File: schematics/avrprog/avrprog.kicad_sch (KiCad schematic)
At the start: 37 parts, among them J1 USB_B, J2 AVR-ISP-10, J3 PROG_PWR, J4 EMCLK, J5 SELF_PROG, U1 FT232RL, U2 ATmega8A-P, Y1 16MHz

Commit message: schematic ...
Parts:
- D8: value PPWRLED -> PWRLED
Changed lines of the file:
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@@
   (junction (at 180.34 43.18) (diameter 0) (color 0 0 0 0)
+  )
+  (junction (at 35.56 67.31) (diameter 0) (color 0 0 0 0)
   )
   (junction (at 196.85 27.94) (diameter 0) (color 0 0 0 0)
@@
     (pin "1")
   )
-  (symbol (lib_id "power:VCC") (at 52.07 69.85 0) (unit 1)
-    (in_bom yes) (on_board yes) (fields_autoplaced)
-    (property "Reference" "#PWR02" (id 0) (at 52.07 73.66 0)
-      (effects (font (size 1.27 1.27)) hide)
-    )
-    (property "Value" "VCC" (id 1) (at 52.07 64.77 0))
+  (symbol (lib_id "power:VCC") (at 52.07 69.85 270) (unit 1)
+    (in_bom yes) (on_board yes) (fields_autoplaced)
+    (property "Reference" "#PWR02" (id 0) (at 48.26 69.85 0)
+      (effects (font (size 1.27 1.27)) hide)
+    )
+    (property "Value" "VCC" (id 1) (at 55.88 69.8499 90)
+      (effects (font (size 1.27 1.27)) (justify left))
+    )
     (property "Footprint" "" (id 2) (at 52.07 69.85 0)
       (effects (font (size 1.27 1.27)) hide)
@@
     )
     (property "Datasheet" "" (id 3) (at 81.28 124.46 0)
+      (effects (font (size 1.27 1.27)) hide)
+    )
+    (pin "1")
+  )
+  (symbol (lib_id "power:PWR_FLAG") (at 35.56 67.31 0) (unit 1)
+    (in_bom yes) (on_board yes) (fields_autoplaced)
+    (property "Reference" "#FLG0102" (id 0) (at 35.56 65.405 0)
+      (effects (font (size 1.27 1.27)) hide)
+    )
+    (property "Value" "PWR_FLAG" (id 1) (at 38.1 66.0399 0)
+      (effects (font (size 1.27 1.27)) (justify left))
+    )
+    (property "Footprint" "" (id 2) (at 35.56 67.31 0)
+      (effects (font (size 1.27 1.27)) hide)
+    )
+    (property "Datasheet" "~" (id 3) (at 35.56 67.31 0)
       (effects (font (size 1.27 1.27)) hide)
     )
@@
       (effects (font (size 1.27 1.27)) (justify right))
     )
-    (property "Value" "PPWRLED" (id 1) (at 52.07 118.4274 90)
+    (property "Value" "PWRLED" (id 1) (at 52.07 118.4274 90)
       (effects (font (size 1.27 1.27)) (justify right))
     )
@@
       (reference "#FLG0101") (unit 1) (value "PWR_FLAG") (footprint "")
     )
+    (path "/51a1c586-d1f4-4b83-b720-2322c5faf689"
+      (reference "#FLG0102") (unit 1) (value "PWR_FLAG") (footprint "")
+    )
     (path "/b570ab2f-b9f6-411e-9c83-e8f97ef2f65d"
       (reference "#PWR01") (unit 1) (value "GND") (footprint "")
@@
     )
     (path "/be34b9bd-279e-4787-9dc2-e7492296784e"
-      (reference "D8") (unit 1) (value "PPWRLED") (footprint "LED_THT:LED_D3.0mm")
+      (reference "D8") (unit 1) (value "PWRLED") (footprint "LED_THT:LED_D3.0mm")
     )
     (path "/727ac96a-3f0b-4596-8661-4535112a64e9"

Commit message: schematic ...
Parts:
- added C10: 100nF, Capacitor_THT:C_Disc_D3.8mm_W2.6mm_P2.50mm, symbol Device:C
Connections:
- net GND: now also C10.1
- net VCC: now also C10.2
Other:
- moved on the sheet: C1, C3, C4, D8, R11

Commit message: schematics completed
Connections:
- net CTS_AT# renamed RTS_FT232#
- net RTS_FT232#: no longer U2.5 (PD3)
- net CTS_FT232#: no longer names the net of U1.11 (CTS)
- net CTS_FT232#: no longer U2.4 (PD2)
- net RXD_AT renamed TXD_FT232
- no-connect marks 15 -> 18
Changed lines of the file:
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@@
   (junction (at 196.85 27.94) (diameter 0) (color 0 0 0 0)
   )
+  (no_connect (at 214.63 105.41))
   (no_connect (at 116.84 69.85))
   (no_connect (at 116.84 87.63))
@@
   (no_connect (at 214.63 85.09))
   (no_connect (at 76.2 74.93))
+  (no_connect (at 214.63 107.95))
   (no_connect (at 214.63 82.55))
   (no_connect (at 214.63 64.77))
   (no_connect (at 214.63 110.49))
+  (no_connect (at 116.84 64.77))
   (no_connect (at 116.84 90.17))
   (no_connect (at 76.2 85.09))
@@
   (no_connect (at 214.63 69.85))
   (no_connect (at 76.2 80.01))
-  (wire (pts (xy 254 99.06) (xy 266.7 99.06))
-    (stroke (width 0) (type default) (color 0 0 0 0))
-  )
   (wire (pts (xy 254 76.2) (xy 256.54 76.2))
     (stroke (width 0) (type default) (color 0 0 0 0))
@@
     (stroke (width 0) (type default) (color 0 0 0 0))
   )
-  (wire (pts (xy 254 96.52) (xy 266.7 96.52))
-    (stroke (width 0) (type default) (color 0 0 0 0))
-  )
   (wire (pts (xy 254 81.28) (xy 256.54 81.28))
     (stroke (width 0) (type default) (color 0 0 0 0))
@@
   )
   (wire (pts (xy 172.72 35.56) (xy 172.72 43.18))
-    (stroke (width 0) (type default) (color 0 0 0 0))
-  )
-  (wire (pts (xy 254 101.6) (xy 266.7 101.6))
-    (stroke (width 0) (type default) (color 0 0 0 0))
-  )
-  (wire (pts (xy 254 93.98) (xy 266.7 93.98))
     (stroke (width 0) (type default) (color 0 0 0 0))
   )
@@
   (label "MOSI_AT" (at 266.7 78.74 0)
     (effects (font (size 1.27 1.27)) (justify left bottom))
-  )
-  (label "RTS_FT232#" (at 254 101.6 180)
-    (effects (font (size 1.27 1.27)) (justify right bottom))
   )
   (label "TXLED#" (at 116.84 82.55 0)
@@
     (effects (font (size 1.27 1.27)) (justify left bottom))
   )
-  (label "TXD_FT232" (at 254 93.98 180)
-    (effects (font (size 1.27 1.27)) (justify right bottom))
+  (label "TXD_FT232" (at 214.63 100.33 0)
+    (effects (font (size 1.27 1.27)) (justify left bottom))
   )
   (label "USB_D-" (at 76.2 67.31 180)
@@
     (effects (font (size 1.27 1.27)) (justify left bottom))
   )
-  (label "RTS_AT#" (at 214.63 105.41 0)
-    (effects (font (size 1.27 1.27)) (justify left bottom))
-  )
   (label "RXD_FT232" (at 254 76.2 180)
     (effects (font (size 1.27 1.27)) (justify right bottom))
@@
   (label "RTS_FT232#" (at 254 78.74 180)
     (effects (font (size 1.27 1.27)) (justify right bottom))
-  )
-  (label "TXD_AT" (at 266.7 96.52 0)
-    (effects (font (size 1.27 1.27)) (justify left bottom))
   )
   (label "SCK_PRG" (at 265.43 46.99 0)
@@
   )
   (label "RXLED#" (at 116.84 85.09 0)
-    (effects (font (size 1.27 1.27)) (justify left bottom))
-  )
-  (label "RXD_AT" (at 214.63 100.33 0)
     (effects (font (size 1.27 1.27)) (justify left bottom))
   )
@@
     (effects (font (size 1.27 1.27)) (justify left bottom))
   )
-  (label "CTS_FT232#" (at 116.84 64.77 0)
-    (effects (font (size 1.27 1.27)) (justify left bottom))
-  )
-  (label "CTS_AT#" (at 266.7 101.6 0)
-    (effects (font (size 1.27 1.27)) (justify left bottom))
-  )
   (label "EMCLK_AT" (at 214.63 67.31 0)
     (effects (font (size 1.27 1.27)) (justify left bottom))
@@
     (effects (font (size 1.27 1.27)) (justify left bottom))
   )
-  (label "RXD_AT" (at 266.7 93.98 0)
-    (effects (font (size 1.27 1.27)) (justify left bottom))
-  )
   (label "GREEN_AT" (at 214.63 118.11 0)
     (effects (font (size 1.27 1.27)) (justify left bottom))
@@
   (label "TXD_FT232" (at 116.84 57.15 0)
     (effects (font (size 1.27 1.27)) (justify left bottom))
-  )
-  (label "CTS_FT232#" (at 254 99.06 180)
-    (effects (font (size 1.27 1.27)) (justify right bottom))
   )
   (label "USB_D-" (at 35.56 72.39 0)
@@
     (effects (font (size 1.27 1.27)) (justify left bottom))
   )
-  (label "RXD_FT232" (at 254 96.52 180)
-    (effects (font (size 1.27 1.27)) (justify right bottom))
+  (label "RXD_FT232" (at 214.63 102.87 0)
+    (effects (font (size 1.27 1.27)) (justify left bottom))
   )
   (label "MOSI_PRG" (at 265.43 44.45 0)
-    (effects (font (size 1.27 1.27)) (justify left bottom))
-  )
-  (label "CTS_AT#" (at 214.63 107.95 0)
-    (effects (font (size 1.27 1.27)) (justify left bottom))
-  )
-  (label "TXD_AT" (at 214.63 102.87 0)
     (effects (font (size 1.27 1.27)) (justify left bottom))
   )
@@
     (effects (font (size 1.27 1.27)) (justify left bottom))
   )
-  (label "RTS_AT#" (at 266.7 99.06 0)
-    (effects (font (size 1.27 1.27)) (justify left bottom))
-  )

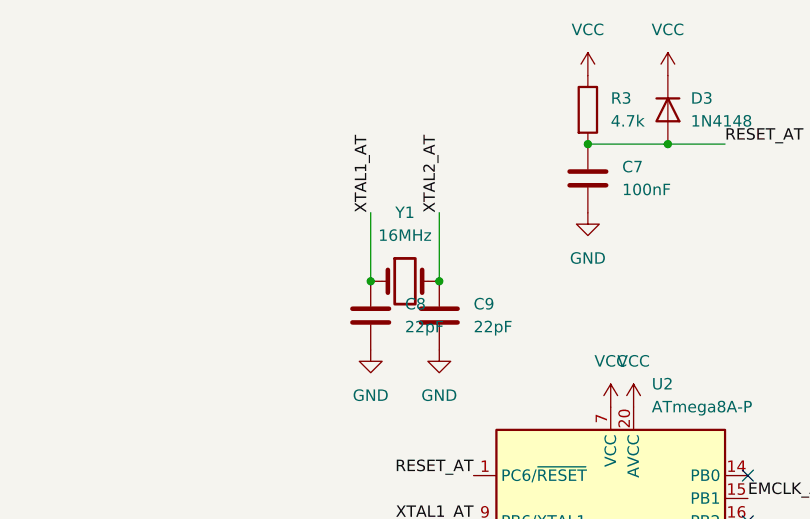
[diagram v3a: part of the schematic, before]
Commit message: crystal changed from 16MHz to 14.7456MHz due to USART communication
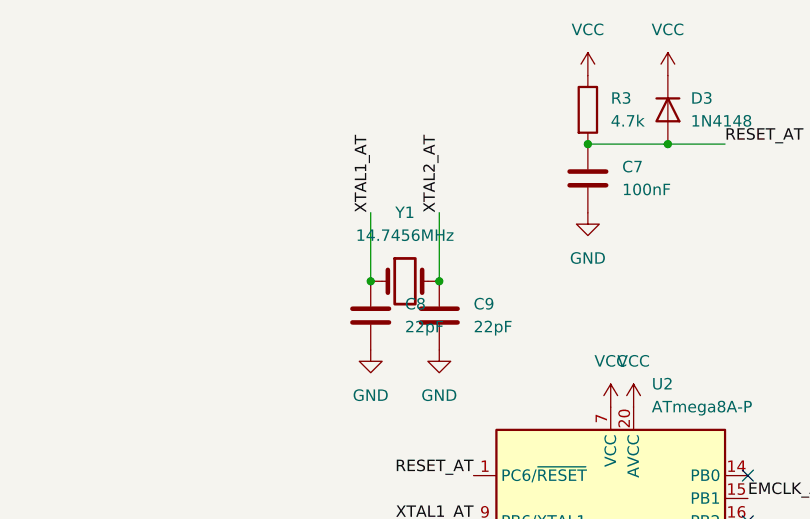
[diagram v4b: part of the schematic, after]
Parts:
- Y1: value 16MHz -> 14.7456MHz
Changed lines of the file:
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@@
     (in_bom yes) (on_board yes) (fields_autoplaced)
     (property "Reference" "Y1" (id 0) (at 176.53 35.56 0))
-    (property "Value" "16MHz" (id 1) (at 176.53 38.1 0))
+    (property "Value" "14.7456MHz" (id 1) (at 176.53 38.1 0))
     (property "Footprint" "Crystal:Crystal_HC49-U_Vertical" (id 2) (at 176.53 43.18 0)
       (effects (font (size 1.27 1.27)) hide)
     )
-    (property "Datasheet" "https://www.hestore.hu/prod_10021423.html" (id 3) (at 176.53 43.18 0)
+    (property "Datasheet" "https://www.hestore.hu/prod_10025226.html" (id 3) (at 176.53 43.18 0)
       (effects (font (size 1.27 1.27)) hide)
     )
@@
     )
     (path "/b62db5c2-6a16-4e7b-8e99-cc24d6f8d94d"
-      (reference "Y1") (unit 1) (value "16MHz") (footprint "Crystal:Crystal_HC49-U_Vertical")
-    )
-  )
+      (reference "Y1") (unit 1) (value "14.7456MHz") (footprint "Crystal:Crystal_HC49-U_Vertical")
+    )
+  )

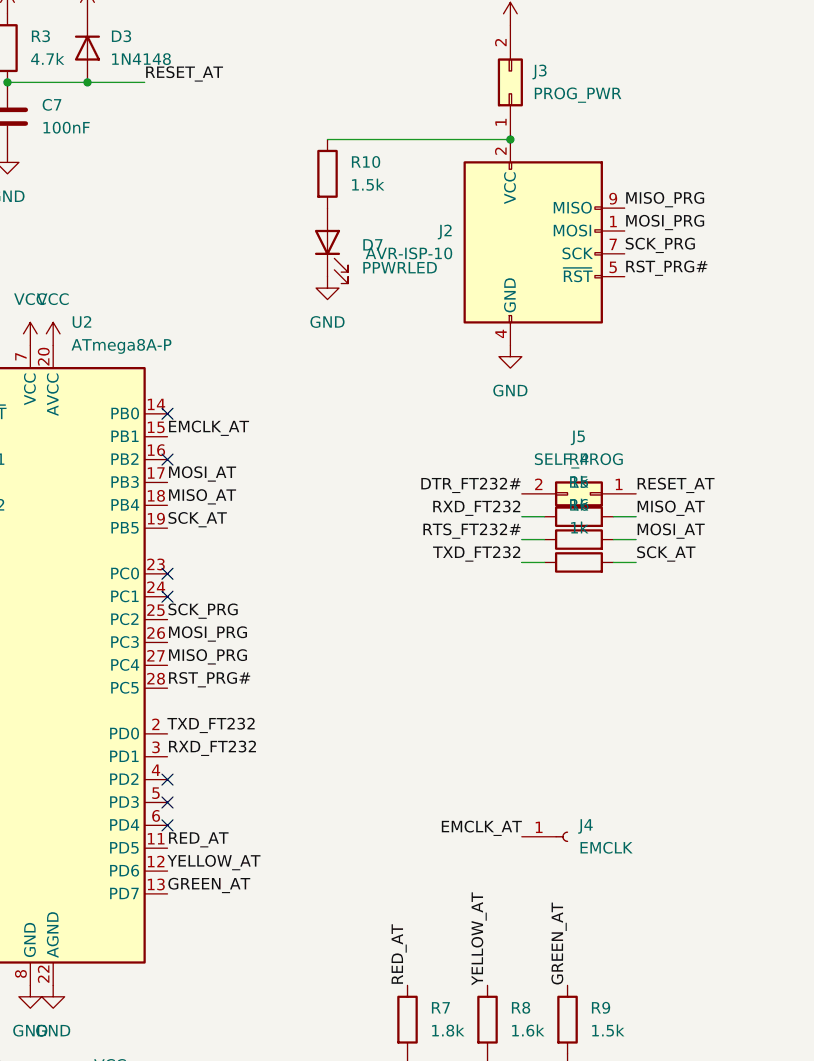
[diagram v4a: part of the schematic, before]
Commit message: PCB reorganized
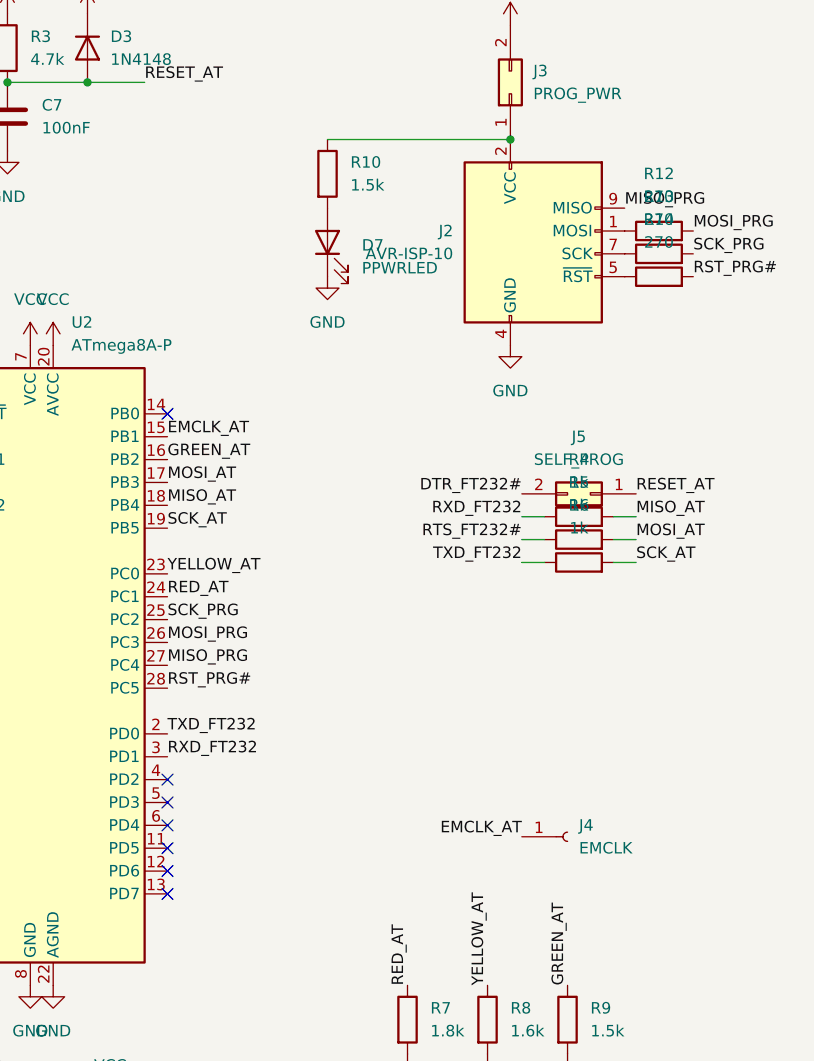
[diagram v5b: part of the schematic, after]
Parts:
- added R12, R13, R14: 270, Resistor_THT:R_Axial_DIN0207_L6.3mm_D2.5mm_P10.16mm_Horizontal, symbol Device:R
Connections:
- net GREEN_AT: now also U2.16 (PB2); no longer U2.13 (PD7)
- net MOSI_PRG: now also R12.2; no longer J2.1 (MOSI)
- net RED_AT: now also U2.24 (PC1); no longer U2.11 (PD5)
- net RST_PRG#: now also R14.2; no longer J2.5 (~{RST})
- net SCK_PRG: now also R13.2; no longer J2.7 (SCK)
- net YELLOW_AT: now also U2.23 (PC0); no longer U2.12 (PD6)
- new net: J2.7 (SCK), R13.1
- new net: J2.1 (MOSI), R12.1
- new net: J2.5 (~{RST}), R14.1
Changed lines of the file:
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@@
   (no_connect (at 184.15 80.01))
   (no_connect (at 116.84 74.93))
-  (no_connect (at 214.63 85.09))
+  (no_connect (at 214.63 115.57))
   (no_connect (at 76.2 74.93))
   (no_connect (at 214.63 107.95))
-  (no_connect (at 214.63 82.55))
+  (no_connect (at 214.63 113.03))
   (no_connect (at 214.63 64.77))
   (no_connect (at 214.63 110.49))
@@
   (no_connect (at 76.2 85.09))
   (no_connect (at 116.84 72.39))
-  (no_connect (at 214.63 69.85))
+  (no_connect (at 214.63 118.11))
   (no_connect (at 76.2 80.01))
   (wire (pts (xy 254 76.2) (xy 256.54 76.2))
@@
     (effects (font (size 1.27 1.27)) (justify left bottom))
   )
-  (label "YELLOW_AT" (at 214.63 115.57 0)
+  (label "YELLOW_AT" (at 214.63 82.55 0)
     (effects (font (size 1.27 1.27)) (justify left bottom))
   )
@@
     (effects (font (size 1.27 1.27)) (justify left bottom))
   )
-  (label "RED_AT" (at 214.63 113.03 0)
+  (label "RED_AT" (at 214.63 85.09 0)
     (effects (font (size 1.27 1.27)) (justify left bottom))
   )
@@
     (effects (font (size 1.27 1.27)) (justify left bottom))
   )
-  (label "RST_PRG#" (at 265.43 49.53 0)
+  (label "RST_PRG#" (at 273.05 49.53 0)
     (effects (font (size 1.27 1.27)) (justify left bottom))
   )
@@
     (effects (font (size 1.27 1.27)) (justify right bottom))
   )
-  (label "SCK_PRG" (at 265.43 46.99 0)
+  (label "SCK_PRG" (at 273.05 46.99 0)
     (effects (font (size 1.27 1.27)) (justify left bottom))
   )
@@
     (effects (font (size 1.27 1.27)) (justify left bottom))
   )
-  (label "GREEN_AT" (at 214.63 118.11 0)
+  (label "GREEN_AT" (at 214.63 69.85 0)
     (effects (font (size 1.27 1.27)) (justify left bottom))
   )
@@
     (effects (font (size 1.27 1.27)) (justify left bottom))
   )
-  (label "MOSI_PRG" (at 265.43 44.45 0)
+  (label "MOSI_PRG" (at 273.05 44.45 0)
     (effects (font (size 1.27 1.27)) (justify left bottom))
   )
@@
   (label "MISO_AT" (at 266.7 76.2 0)
     (effects (font (size 1.27 1.27)) (justify left bottom))
+  )
+  (symbol (lib_id "Device:R") (at 269.24 46.99 90) (unit 1)
+    (in_bom yes) (on_board yes) (fields_autoplaced)
+    (property "Reference" "R13" (id 0) (at 269.24 40.64 90))
+    (property "Value" "270" (id 1) (at 269.24 43.18 90))
+    (property "Footprint" "Resistor_THT:R_Axial_DIN0207_L6.3mm_D2.5mm_P10.16mm_Horizontal" (id 2) (at 269.24 48.768 90)
+      (effects (font (size 1.27 1.27)) hide)
+    )
+    (property "Datasheet" "https://www.hestore.hu/prod_10020502.html" (id 3) (at 269.24 46.99 0)
+      (effects (font (size 1.27 1.27)) hide)
+    )
+    (pin "1")
+    (pin "2")
   )
   (symbol (lib_id "power:VCC") (at 196.85 20.32 0) (unit 1)
@@
     (pin "1")
   )
+  (symbol (lib_id "Device:R") (at 269.24 44.45 90) (unit 1)
+    (in_bom yes) (on_board yes) (fields_autoplaced)
+    (property "Reference" "R12" (id 0) (at 269.24 38.1 90))
+    (property "Value" "270" (id 1) (at 269.24 40.64 90))
+    (property "Footprint" "Resistor_THT:R_Axial_DIN0207_L6.3mm_D2.5mm_P10.16mm_Horizontal" (id 2) (at 269.24 46.228 90)
+      (effects (font (size 1.27 1.27)) hide)
+    )
+    (property "Datasheet" "https://www.hestore.hu/prod_10020502.html" (id 3) (at 269.24 44.45 0)
+      (effects (font (size 1.27 1.27)) hide)
+    )
+    (pin "1")
+    (pin "2")
+  )
   (symbol (lib_id "power:VCC") (at 88.9 115.57 0) (unit 1)
     (in_bom yes) (on_board yes) (fields_autoplaced)
@@
     )
     (property "Datasheet" "https://www.hestore.hu/prod_10020523.html" (id 3) (at 241.3 132.08 0)
+      (effects (font (size 1.27 1.27)) hide)
+    )
+    (pin "1")
+    (pin "2")
+  )
+  (symbol (lib_id "Device:R") (at 269.24 49.53 90) (unit 1)
+    (in_bom yes) (on_board yes) (fields_autoplaced)
+    (property "Reference" "R14" (id 0) (at 269.24 43.18 90))
+    (property "Value" "270" (id 1) (at 269.24 45.72 90))
+    (property "Footprint" "Resistor_THT:R_Axial_DIN0207_L6.3mm_D2.5mm_P10.16mm_Horizontal" (id 2) (at 269.24 51.308 90)
+      (effects (font (size 1.27 1.27)) hide)
+    )
+    (property "Datasheet" "https://www.hestore.hu/prod_10020502.html" (id 3) (at 269.24 49.53 0)
       (effects (font (size 1.27 1.27)) hide)
     )
@@
       (reference "R11") (unit 1) (value "1.5k") (footprint "Resistor_THT:R_Axial_DIN0207_L6.3mm_D2.5mm_P10.16mm_Horizontal")
     )
+    (path "/69b97e2b-5110-41b1-87c9-a936f0563d7f"
+      (reference "R12") (unit 1) (value "270") (footprint "Resistor_THT:R_Axial_DIN0207_L6.3mm_D2.5mm_P10.16mm_Horizontal")
+    )
+    (path "/01e17cfe-6ba2-4c20-a668-ce268d3ed1b1"
+      (reference "R13") (unit 1) (value "270") (footprint "Resistor_THT:R_Axial_DIN0207_L6.3mm_D2.5mm_P10.16mm_Horizontal")
+    )
+    (path "/9cbc4c4a-e55c-4106-9ef2-29d63e541e42"
+      (reference "R14") (unit 1) (value "270") (footprint "Resistor_THT:R_Axial_DIN0207_L6.3mm_D2.5mm_P10.16mm_Horizontal")
+    )
     (path "/136955f2-929a-406d-a07c-852746ff0c88"
